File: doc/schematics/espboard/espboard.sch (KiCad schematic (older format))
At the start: 13 parts, among them J1 Conn_01x02, J2 Stripe Data, J3 RPi Serial, J4 Conn_01x10, U1 ESP32DEVKITV1, U2 SN74HCT245N

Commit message: Updated schematics
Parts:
- added C?: 1µF, symbol Device:CP
- J1: value Conn_01x02 -> PWR
- J4: value Conn_01x10 -> Upper Board
- U1: footprint ESP32-DEVKITV1 -> ESP32-DEVKITV1:ESP32-DEVKITV1
- U2: footprint Texas_Instruments-SN74HCT245N-0-0-* -> eec:Texas_Instruments-SN74HCT245N-0-0-MFG
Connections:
- net +5V: now also C?.1
- net GND: now also C?.2
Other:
- note removed: "Value TODO"
- moved on the sheet: J1
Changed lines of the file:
@@
 P 1900 2000
 F 0 "J4" V 2117 1946 50  0000 C CNN
-F 1 "Conn_01x10" V 2026 1946 50  0000 C CNN
+F 1 "Upper Board" V 2026 1946 50  0000 C CNN
 F 2 "" H 1900 2000 50  0001 C CNN
 F 3 "~" H 1900 2000 50  0001 C CNN
@@
 F 0 "U1" V 4859 3600 50  0000 C CNN
 F 1 "ESP32DEVKITV1" H 4050 3600 50  0001 L BNN
-F 2 "ESP32-DEVKITV1" H 4050 3600 50  0001 L BNN
+F 2 "ESP32-DEVKITV1:ESP32-DEVKITV1" H 4050 3600 50  0001 L BNN
 F 3 "" H 4050 3600 50  0001 C CNN
 	1    4050 3600
@@
 L Connector_Generic:Conn_01x02 J1
 U 1 1 5F7C4D16
-P 6100 1500
-F 0 "J1" H 6180 1446 50  0000 L CNN
-F 1 "Conn_01x02" H 6180 1401 50  0001 L CNN
-F 2 "" H 6100 1500 50  0001 C CNN
-F 3 "~" H 6100 1500 50  0001 C CNN
-	1    6100 1500
-	1    0    0    -1
-$EndComp
-$Comp
-L power:GND #PWR0101
-U 1 1 5F7CC7B9
-P 5050 4650
-F 0 "#PWR0101" H 5050 4400 50  0001 C CNN
-F 1 "GND" H 5055 4477 50  0000 C CNN
-F 2 "" H 5050 4650 50  0001 C CNN
-F 3 "" H 5050 4650 50  0001 C CNN
-	1    5050 4650
+P 6800 1300
+F 0 "J1" H 6880 1246 50  0000 L CNN
+F 1 "PWR" H 6900 1150 50  0000 L CNN
+F 2 "" H 6800 1300 50  0001 C CNN
+F 3 "~" H 6800 1300 50  0001 C CNN
+	1    6800 1300
 	1    0    0    -1
 $EndComp
@@
 L power:GND #PWR0104
 U 1 1 5F7DE56A
-P 5750 1700
-F 0 "#PWR0104" H 5750 1450 50  0001 C CNN
-F 1 "GND" H 5755 1527 50  0000 C CNN
-F 2 "" H 5750 1700 50  0001 C CNN
-F 3 "" H 5750 1700 50  0001 C CNN
-	1    5750 1700
-	1    0    0    -1
-$EndComp
-Wire Wire Line
-	5750 1700 5750 1600
-Wire Wire Line
-	5750 1400 5750 1500
+P 6450 1650
+F 0 "#PWR0104" H 6450 1400 50  0001 C CNN
+F 1 "GND" H 6455 1477 50  0000 C CNN
+F 2 "" H 6450 1650 50  0001 C CNN
+F 3 "" H 6450 1650 50  0001 C CNN
+	1    6450 1650
+	1    0    0    -1
+$EndComp
+Wire Wire Line
+	6450 1650 6450 1500
+Wire Wire Line
+	6450 1050 6450 1200
 $Comp
 L power:+5V #PWR0105
 U 1 1 5F7DFD8C
-P 5750 1400
-F 0 "#PWR0105" H 5750 1250 50  0001 C CNN
-F 1 "+5V" H 5765 1573 50  0000 C CNN
-F 2 "" H 5750 1400 50  0001 C CNN
-F 3 "" H 5750 1400 50  0001 C CNN
-	1    5750 1400
+P 6450 1050
+F 0 "#PWR0105" H 6450 900 50  0001 C CNN
+F 1 "+5V" H 6465 1223 50  0000 C CNN
+F 2 "" H 6450 1050 50  0001 C CNN
+F 3 "" H 6450 1050 50  0001 C CNN
+	1    6450 1050
 	1    0    0    -1
 $EndComp
@@
 	1    0    0    -1
 $EndComp
-Wire Wire Line
-	5050 4650 5050 4400
 Wire Wire Line
 	5050 4400 4750 4400
@@
 	1    0    0    -1
 $EndComp
-Wire Wire Line
-	3000 4500 3350 4500
 $Comp
 L Connector_Generic:Conn_01x02 J3
@@
 Wire Wire Line
 	2900 2850 2900 1900
-Text Notes 2550 3200 0    50   ~ 0
-Value TODO
 $Comp
 L Device:R R5
@@
 F 0 "U2" H 8600 2135 50  0000 C CNN
 F 1 "SN74HCT245N" H 8600 2226 50  0000 C CNN
-F 2 "Texas_Instruments-SN74HCT245N-0-0-*" H 7900 4500 50  0001 L CNN
+F 2 "eec:Texas_Instruments-SN74HCT245N-0-0-MFG" H 7900 4500 50  0001 L CNN
 F 3 "http://www.ti.com/lit/ds/symlink/sn74hct245.pdf" H 7900 4600 50  0001 L CNN
 F 4 "+85°C" H 7900 4700 50  0001 L CNN "ambient temperature range high"
@@
 L power:PWR_FLAG #FLG0101
 U 1 1 5F8DE5CC
-P 5750 1500
-F 0 "#FLG0101" H 5750 1575 50  0001 C CNN
-F 1 "PWR_FLAG" H 5750 1673 50  0001 C CNN
-F 2 "" H 5750 1500 50  0001 C CNN
-F 3 "~" H 5750 1500 50  0001 C CNN
-	1    5750 1500
+P 6450 1300
+F 0 "#FLG0101" H 6450 1375 50  0001 C CNN
+F 1 "PWR_FLAG" H 6450 1473 50  0001 C CNN
+F 2 "" H 6450 1300 50  0001 C CNN
+F 3 "~" H 6450 1300 50  0001 C CNN
+	1    6450 1300
 	0    -1   -1   0
 $EndComp
@@
 L power:PWR_FLAG #FLG0102
 U 1 1 5F90CF4A
-P 5750 1600
-F 0 "#FLG0102" H 5750 1675 50  0001 C CNN
-F 1 "PWR_FLAG" H 5750 1773 50  0001 C CNN
-F 2 "" H 5750 1600 50  0001 C CNN
-F 3 "~" H 5750 1600 50  0001 C CNN
-	1    5750 1600
+P 6450 1400
+F 0 "#FLG0102" H 6450 1475 50  0001 C CNN
+F 1 "PWR_FLAG" H 6450 1573 50  0001 C CNN
+F 2 "" H 6450 1400 50  0001 C CNN
+F 3 "~" H 6450 1400 50  0001 C CNN
+	1    6450 1400
 	0    -1   -1   0
 $EndComp
 Wire Wire Line
-	5750 1500 5900 1500
-Connection ~ 5750 1500
-Wire Wire Line
-	5750 1600 5900 1600
-Connection ~ 5750 1600
+	6450 1300 6600 1300
+Connection ~ 6450 1300
+Wire Wire Line
+	6450 1400 6600 1400
+Connection ~ 6450 1400
 NoConn ~ 4750 4200
+Wire Wire Line
+	5050 4650 5050 4400
+$Comp
+L power:GND #PWR0101
+U 1 1 5F7CC7B9
+P 5050 4650
+F 0 "#PWR0101" H 5050 4400 50  0001 C CNN
+F 1 "GND" H 5055 4477 50  0000 C CNN
+F 2 "" H 5050 4650 50  0001 C CNN
+F 3 "" H 5050 4650 50  0001 C CNN
+	1    5050 4650
+	1    0    0    -1
+$EndComp
+Wire Wire Line
+	3000 4500 3350 4500
+$Comp
+L Device:CP C?
+U 1 1 5F7A73FF
+P 5950 1350
+F 0 "C?" H 6068 1396 50  0000 L CNN
+F 1 "1µF" H 6068 1305 50  0000 L CNN
+F 2 "" H 5988 1200 50  0001 C CNN
+F 3 "~" H 5950 1350 50  0001 C CNN
+	1    5950 1350
+	1    0    0    -1
+$EndComp
+Wire Wire Line
+	5950 1500 6450 1500
+Connection ~ 6450 1500
+Wire Wire Line
+	6450 1500 6450 1400
+Wire Wire Line
+	5950 1200 6450 1200
+Connection ~ 6450 1200
+Wire Wire Line
+	6450 1200 6450 1300
 $EndSCHEMATC

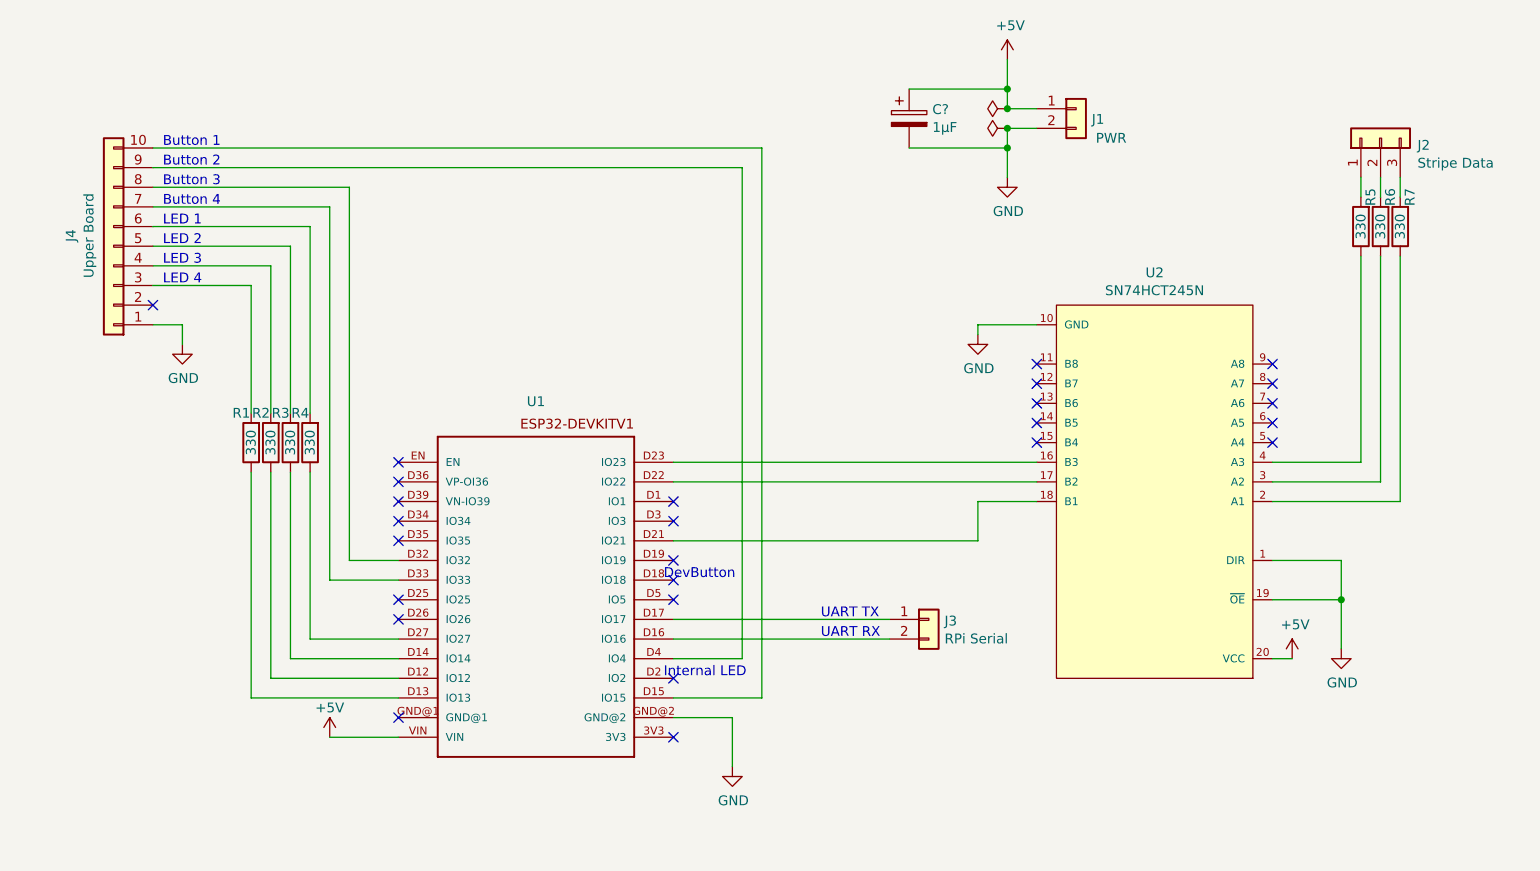
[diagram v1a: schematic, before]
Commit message: Continued schematics
- changed LED resistors to 100 Ohm
- use green leds
- changed stripe data resistors to 150 Ohm
- 10 µF capacitor power buffer
- Boot button exposed to RPi pin header
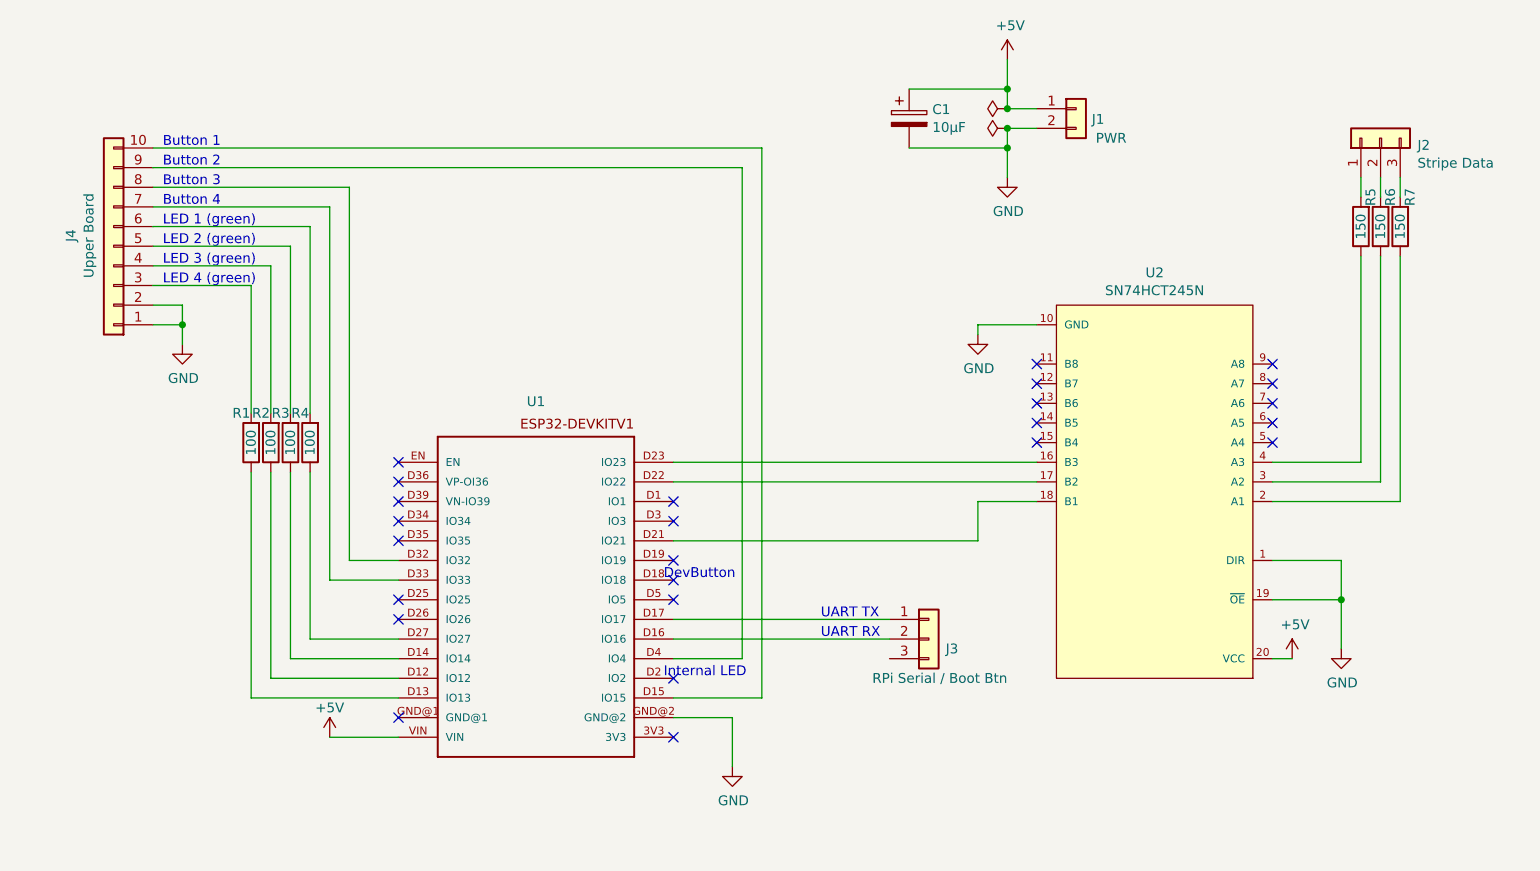
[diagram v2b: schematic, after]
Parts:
- removed J3: RPi Serial, symbol Connector_Generic:Conn_01x02
- added J3: RPi Serial / Boot Btn, symbol Connector_Generic:Conn_01x03
- C1: renamed from C?; value 1µF -> 10µF
- R1, R2, R3, R4: value 330 -> 100
- R5, R6, R7: value 330 -> 150
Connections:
- net GND: now also J4.2 (Pin_2)
- net at U1.D16 (IO16): now also J3.2 (Pin_2)
- net at U1.D17 (IO17): now also J3.1 (Pin_1)
- no-connect marks 26 -> 25
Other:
- note added: "LED 1 (green)"
- note added: "LED 2 (green)"
- note added: "LED 3 (green)"
- note added: "LED 4 (green)"
- note removed: "LED 1"
- note removed: "LED 2"
- note removed: "LED 3"
- note removed: "LED 4"
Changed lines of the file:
@@
-	1    0    0    -1
-$EndComp
-$Comp
-L Connector_Generic:Conn_01x02 J3
-U 1 1 5F80C252
-P 6050 3900
-F 0 "J3" H 6130 3892 50  0000 L CNN
-F 1 "RPi Serial" H 6130 3801 50  0000 L CNN
-F 2 "" H 6050 3900 50  0001 C CNN
-F 3 "~" H 6050 3900 50  0001 C CNN
-	1    6050 3900
 	1    0    0    -1
 $EndComp
@@
 	2700 2100 2100 2100
 Text Notes 2150 1900 0    50   ~ 0
-LED 1
-Text Notes 2150 1500 0    50   ~ 0
-Button 1
+LED 1 (green)
 Text Notes 2150 1600 0    50   ~ 0
 Button 2
@@
 	2600 2200 2100 2200
 Text Notes 2150 2000 0    50   ~ 0
-LED 2
+LED 2 (green)
 $Comp
 L power:GND #PWR0108
@@
 Internal LED
 Text Notes 2150 2100 0    50   ~ 0
-LED 3
+LED 3 (green)
 Text Notes 2150 2200 0    50   ~ 0
-LED 4
+LED 4 (green)
 $Comp
 L Device:R R1
@@
 P 2600 3000
 F 0 "R1" H 2650 2850 50  0000 C CNN
-F 1 "330" V 2600 3000 50  0000 C CNN
+F 1 "100" V 2600 3000 50  0000 C CNN
 F 2 "" V 2530 3000 50  0001 C CNN
 F 3 "~" H 2600 3000 50  0001 C CNN
@@
 P 2700 3000
 F 0 "R2" H 2750 2850 50  0000 C CNN
-F 1 "330" V 2700 3000 50  0000 C CNN
+F 1 "100" V 2700 3000 50  0000 C CNN
 F 2 "" V 2630 3000 50  0001 C CNN
 F 3 "~" H 2700 3000 50  0001 C CNN
@@
 P 2800 3000
 F 0 "R3" H 2850 2850 50  0000 C CNN
-F 1 "330" V 2800 3000 50  0000 C CNN
+F 1 "100" V 2800 3000 50  0000 C CNN
 F 2 "" V 2730 3000 50  0001 C CNN
 F 3 "~" H 2800 3000 50  0001 C CNN
@@
 Wire Wire Line
 	2800 2850 2800 2000
-$Comp
-L Device:R R4
-U 1 1 5F8706D5
-P 2900 3000
-F 0 "R4" H 2950 2850 50  0000 C CNN
-F 1 "330" V 2900 3000 50  0000 C CNN
-F 2 "" V 2830 3000 50  0001 C CNN
-F 3 "~" H 2900 3000 50  0001 C CNN
-	1    2900 3000
-	-1   0    0    1
-$EndComp
 Wire Wire Line
 	2900 2850 2900 1900
@@
 P 8250 1900
 F 0 "R5" V 8200 1750 50  0000 C CNN
-F 1 "330" V 8250 1900 50  0000 C CNN
+F 1 "150" V 8250 1900 50  0000 C CNN
 F 2 "" V 8180 1900 50  0001 C CNN
 F 3 "~" H 8250 1900 50  0001 C CNN
@@
 P 8350 1900
 F 0 "R6" V 8300 1750 50  0000 C CNN
-F 1 "330" V 8350 1900 50  0000 C CNN
+F 1 "150" V 8350 1900 50  0000 C CNN
 F 2 "" V 8280 1900 50  0001 C CNN
 F 3 "~" H 8350 1900 50  0001 C CNN
@@
 P 8450 1900
 F 0 "R7" V 8400 1750 50  0000 C CNN
-F 1 "330" V 8450 1900 50  0000 C CNN
+F 1 "150" V 8450 1900 50  0000 C CNN
 F 2 "" V 8380 1900 50  0001 C CNN
 F 3 "~" H 8450 1900 50  0001 C CNN
@@
 NoConn ~ 3350 3200
 NoConn ~ 3350 3100
-NoConn ~ 2100 2300
 NoConn ~ 3350 4400
 $Comp
@@
 Wire Wire Line
 	5050 4650 5050 4400
+Wire Wire Line
+	3000 4500 3350 4500
+$Comp
+L Device:CP C1
+U 1 1 5F7A73FF
+P 5950 1350
+F 0 "C1" H 6068 1396 50  0000 L CNN
+F 1 "10µF" H 6068 1305 50  0000 L CNN
+F 2 "" H 5988 1200 50  0001 C CNN
+F 3 "~" H 5950 1350 50  0001 C CNN
+	1    5950 1350
+	1    0    0    -1
+$EndComp
+Wire Wire Line
+	5950 1500 6450 1500
+Connection ~ 6450 1500
+Wire Wire Line
+	6450 1500 6450 1400
+Wire Wire Line
+	5950 1200 6450 1200
+Connection ~ 6450 1200
+Wire Wire Line
+	6450 1200 6450 1300
 $Comp
 L power:GND #PWR0101
@@
 $EndComp
 Wire Wire Line
-	3000 4500 3350 4500
-$Comp
-L Device:CP C?
-U 1 1 5F7A73FF
-P 5950 1350
-F 0 "C?" H 6068 1396 50  0000 L CNN
-F 1 "1µF" H 6068 1305 50  0000 L CNN
-F 2 "" H 5988 1200 50  0001 C CNN
-F 3 "~" H 5950 1350 50  0001 C CNN
-	1    5950 1350
-	1    0    0    -1
-$EndComp
-Wire Wire Line
-	5950 1500 6450 1500
-Connection ~ 6450 1500
-Wire Wire Line
-	6450 1500 6450 1400
-Wire Wire Line
-	5950 1200 6450 1200
-Connection ~ 6450 1200
-Wire Wire Line
-	6450 1200 6450 1300
+	2100 2300 2250 2300
+Wire Wire Line
+	2250 2300 2250 2400
+Connection ~ 2250 2400
+$Comp
+L Device:R R4
+U 1 1 5F8706D5
+P 2900 3000
+F 0 "R4" H 2950 2850 50  0000 C CNN
+F 1 "100" V 2900 3000 50  0000 C CNN
+F 2 "" V 2830 3000 50  0001 C CNN
+F 3 "~" H 2900 3000 50  0001 C CNN
+	1    2900 3000
+	-1   0    0    1
+$EndComp
+Text Notes 2150 1500 0    50   ~ 0
+Button 1
+$Comp
+L Connector_Generic:Conn_01x03 J3
+U 1 1 6013BDB3
+P 6050 4000
+F 0 "J3" H 6200 3950 50  0000 R CNN
+F 1 "RPi Serial / Boot Btn" H 6450 3800 50  0000 R CNN
+F 2 "" H 6050 4000 50  0001 C CNN
+F 3 "~" H 6050 4000 50  0001 C CNN
+	1    6050 4000
+	1    0    0    -1
+$EndComp
 $EndSCHEMATC

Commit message: Partyraum schematics: add cable colors for connector
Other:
- note added: "Black"
- note added: "Blue"
- note added: "Brown"
- note added: "Gray"
- note added: "Green"
- note added: "Orange"
- note added: "Purple"
- note added: "Red"
- note added: "White"
- note added: "Yellow"
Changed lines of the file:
@@
 	1    0    0    -1
 $EndComp
+Text Notes 1400 2400 0    50   ~ 0
+Black
+Text Notes 1400 2300 0    50   ~ 0
+Brown
+Text Notes 1400 2200 0    50   ~ 0
+Red
+Text Notes 1400 2100 0    50   ~ 0
+Orange
+Text Notes 1400 2000 0    50   ~ 0
+Yellow
+Text Notes 1400 1900 0    50   ~ 0
+Green
+Text Notes 1400 1800 0    50   ~ 0
+Blue
+Text Notes 1400 1700 0    50   ~ 0
+Purple
+Text Notes 1400 1600 0    50   ~ 0
+Gray
+Text Notes 1400 1500 0    50   ~ 0
+White
 $EndSCHEMATC
